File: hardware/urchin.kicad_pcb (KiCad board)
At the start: 2 copper layers, 19 parts, among them IC1 ATMEGA328PB-A, IC2 ATTINY85-S, P1 CONN_02X03, P2 USB_OTG, U1 CH340G, Y1 12M

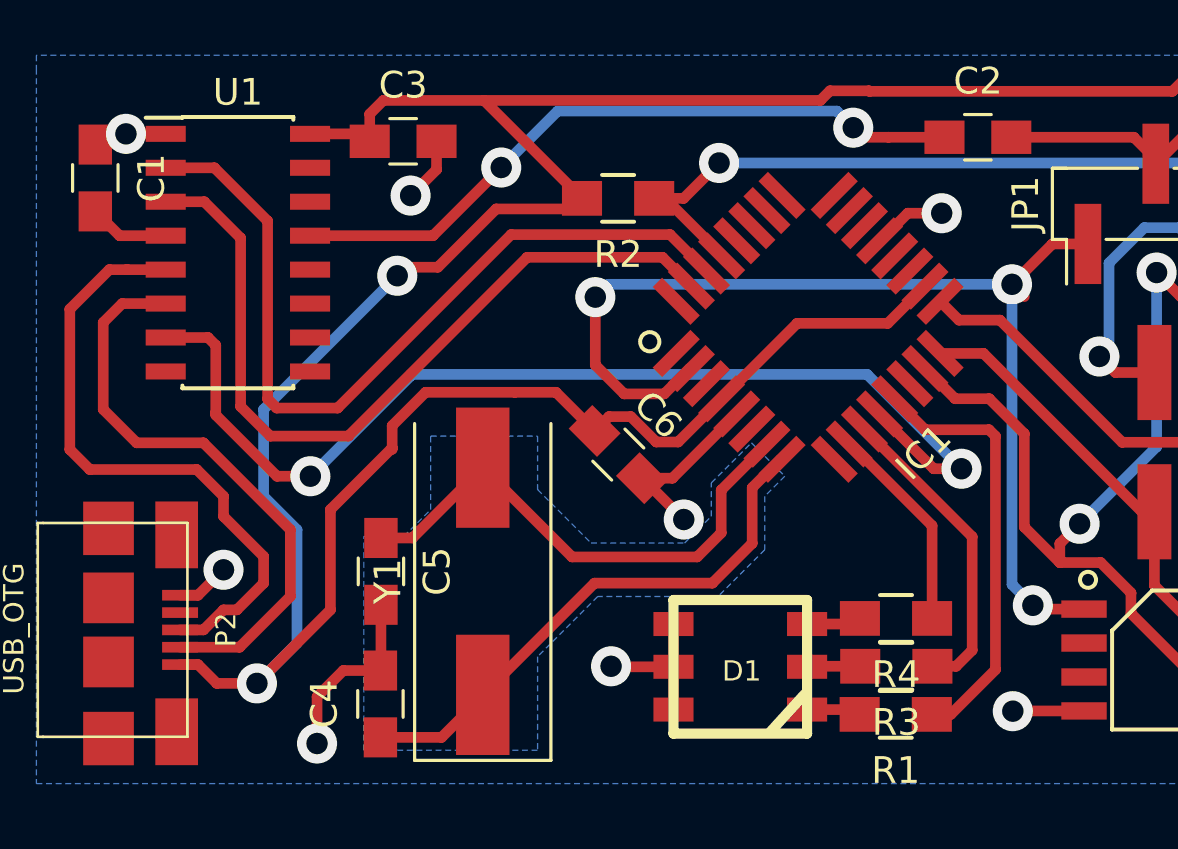
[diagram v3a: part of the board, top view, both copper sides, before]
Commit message: Adding new 100uF reservoir capacitor.
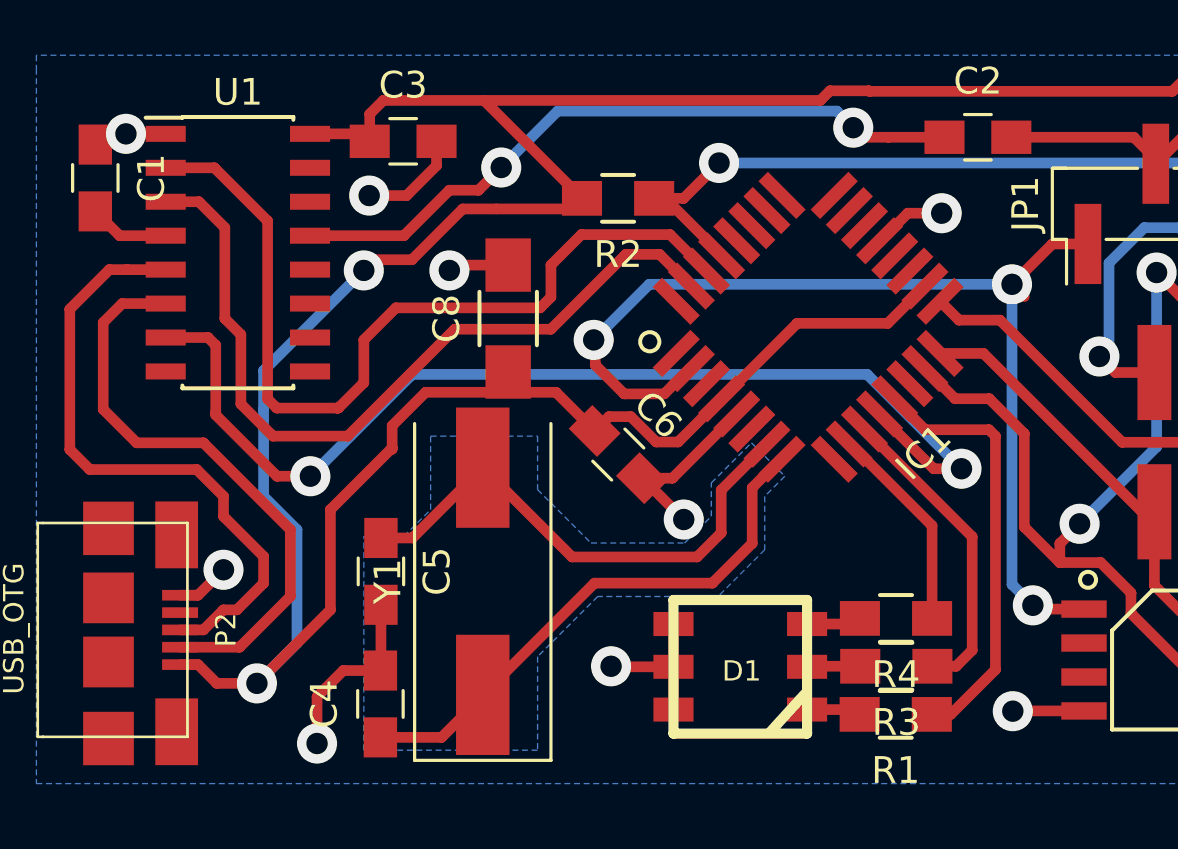
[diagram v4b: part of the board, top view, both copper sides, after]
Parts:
- added C8: 100u, apexelectrix/apex-smd-resistors.pretty:R_1206_HandSoldering, F.Cu at (128.4, 97.2)
- R2: value R_Small -> 10k
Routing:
- net GND: track 37.3 -> 41.1 mm, vias 10 -> 11
- net RXD: track 31.1 -> 32.8 mm
- net RST-PROG: track 41.8 -> 40.9 mm
- net +5V: track 157.5 -> 158.3 mm
